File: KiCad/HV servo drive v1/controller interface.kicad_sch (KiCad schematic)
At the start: 46 parts, among them J8 8P8C_LED_Shielded_x2, M1 Fan_4pin, M2 Fan_4pin, SW2 TERM RES, U2 ISO6721BQDRQ1, U23 THVD1552, U3 ISO6721BQDRQ1, U4 ISO6721BQDRQ1, U6 AP64060QWU-7, U7 WRF0505S-3WR2

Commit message: KiCad 8.0 update
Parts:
- renumbered C95 to C1, C19 to C11, C92 to C13, C1 to C16, C93 to C18, C18 to C19, C11 to C2, C94 to C3, C2 to C31, C13 to C4, C91 to C5, C90 to C6, C16 to C7, C3 to C90, C4 to C91, C31 to C92, C5 to C93, C6 to C94, C7 to C95, J8 to J7, L17 to L1, L1 to L16, L5 to L17, L16 to L5, M2 to M1, M1 to M2, R5 to R1, R6 to R2, R90 to R3, R91 to R4, R4 to R5, R3 to R6, R2 to R79, R1 to R80, U6 to U2, U4 to U23, U23 to U3, U7 to U4, U2 to U6, U3 to U7

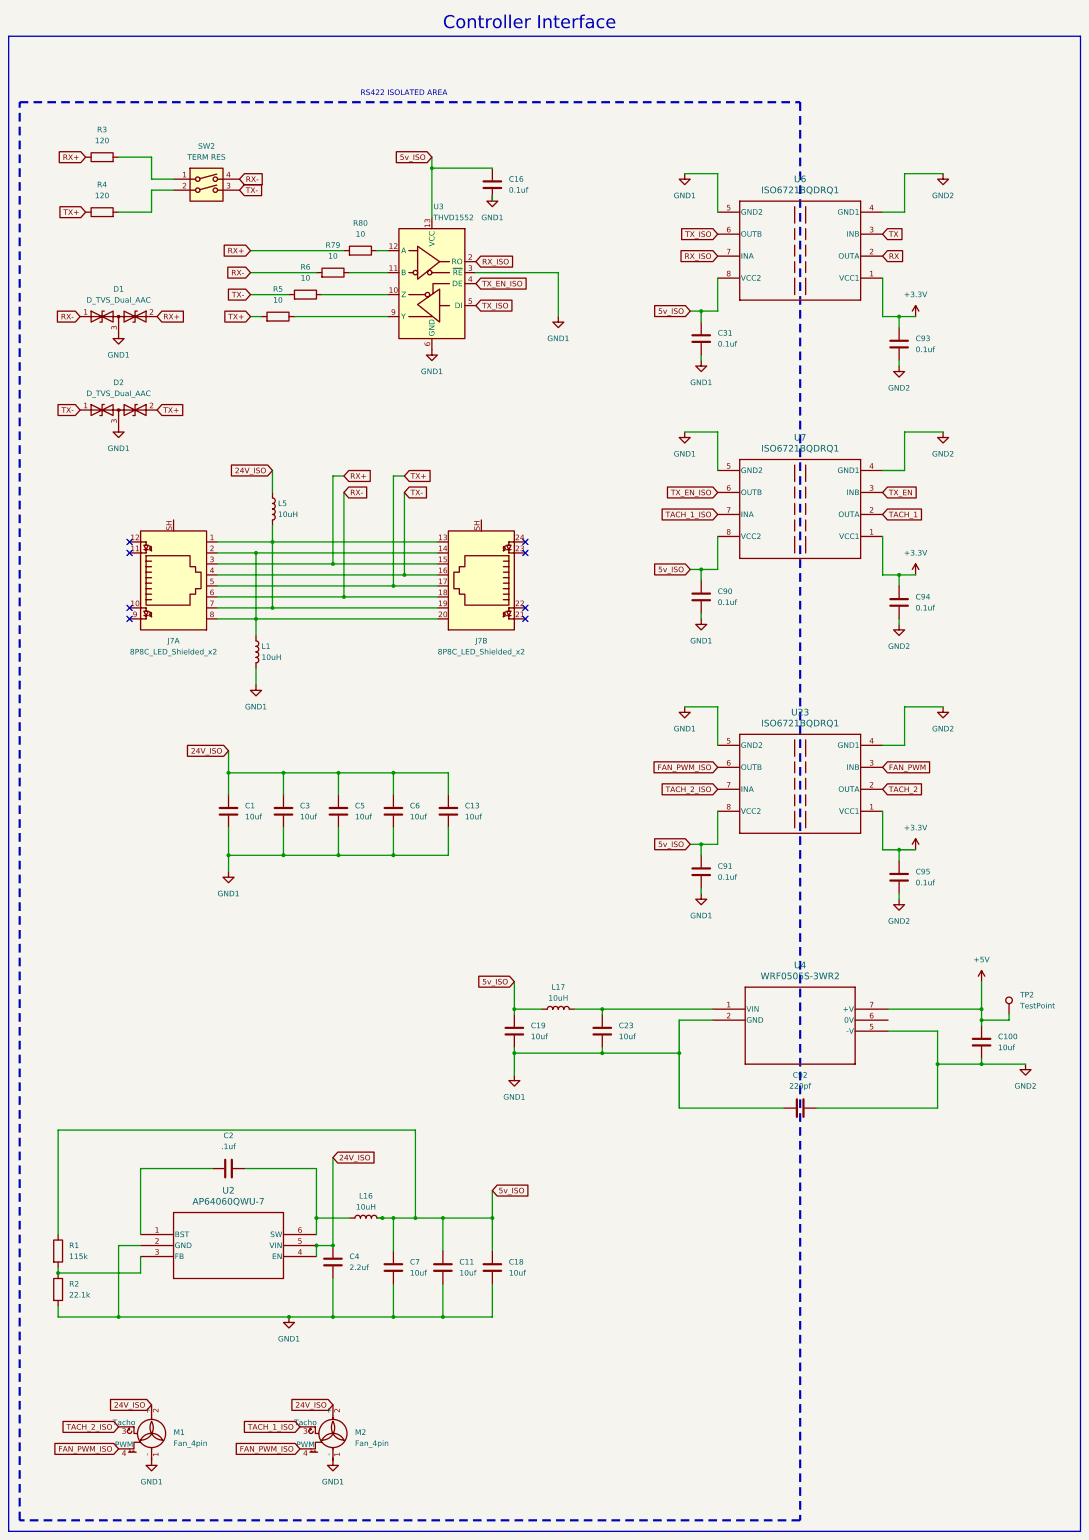
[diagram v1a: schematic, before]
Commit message: start rev 2 changes
fix component references, fix rj45 and dc-dc converter footprints, add RLC filters on all power connectors, add more mounting holes
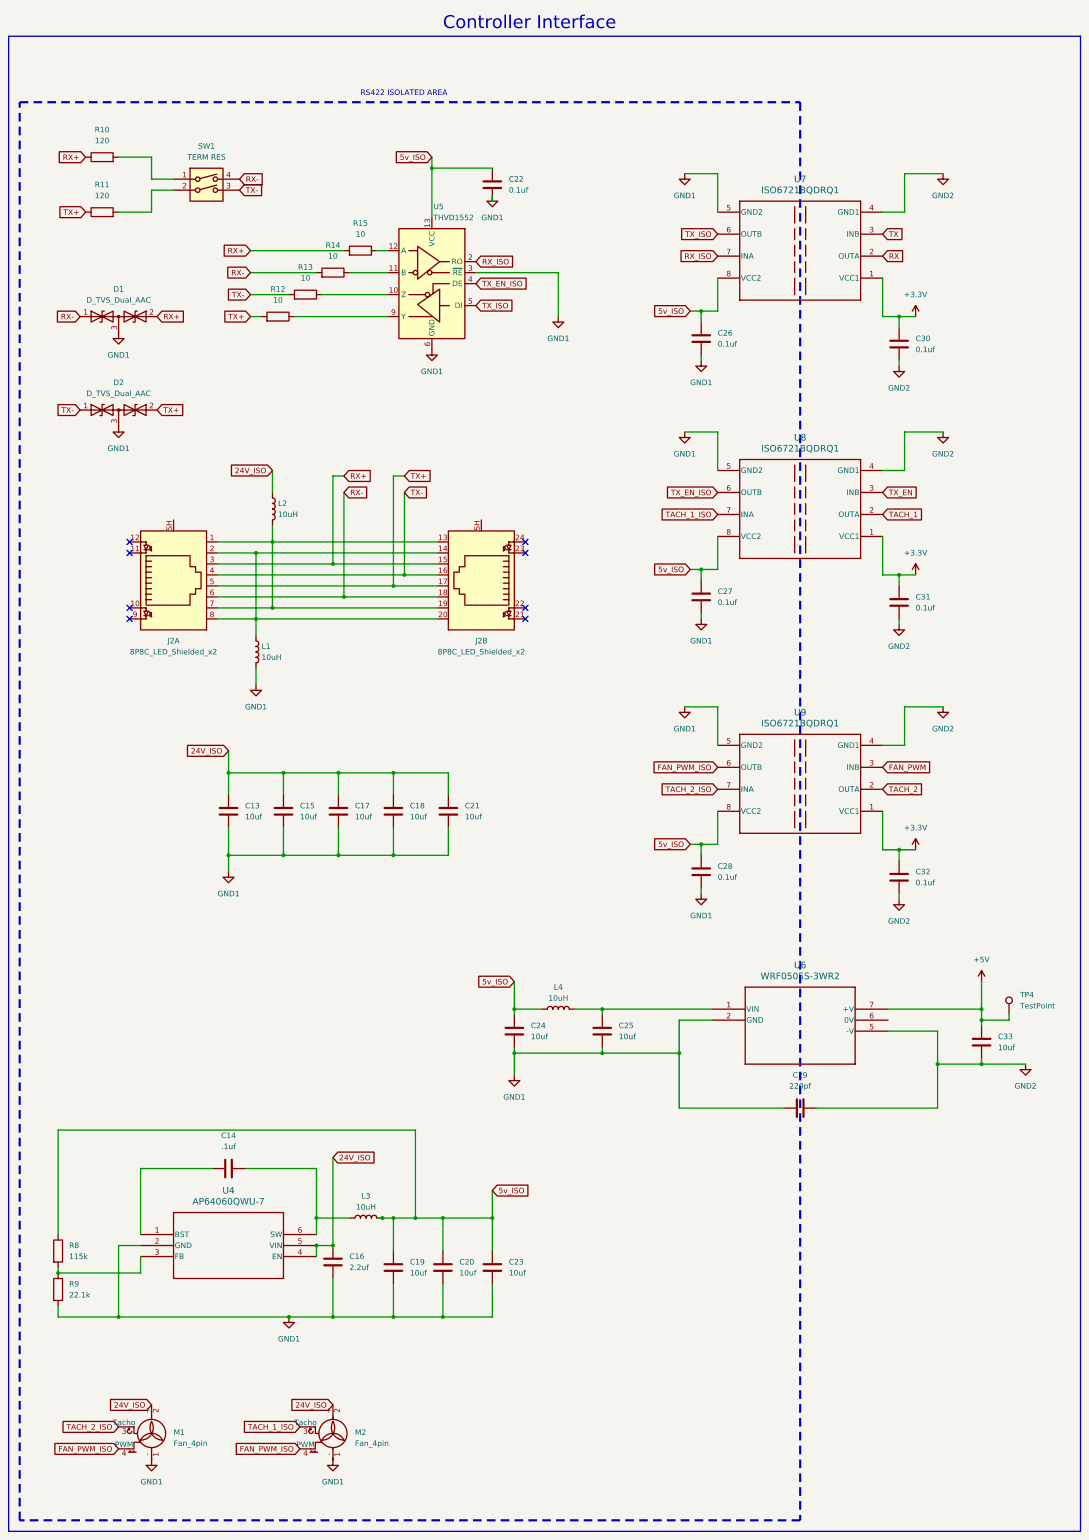
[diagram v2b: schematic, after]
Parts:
- renumbered C1 to C13, C2 to C14, C3 to C15, C4 to C16, C5 to C17, C6 to C18, C7 to C19, C11 to C20, C13 to C21, C16 to C22, C18 to C23, C19 to C24, C23 to C25, C31 to C26, C90 to C27, C91 to C28, C92 to C29, C93 to C30, C94 to C31, C95 to C32, C100 to C33, J7 to J2, L5 to L2, L16 to L3, L17 to L4, R3 to R10, R4 to R11, R5 to R12, R6 to R13, R79 to R14, R80 to R15, R1 to R8, R2 to R9, SW2 to SW1, TP2 to TP4, U2 to U4, U3 to U5, U4 to U6, U6 to U7, U7 to U8, U23 to U9

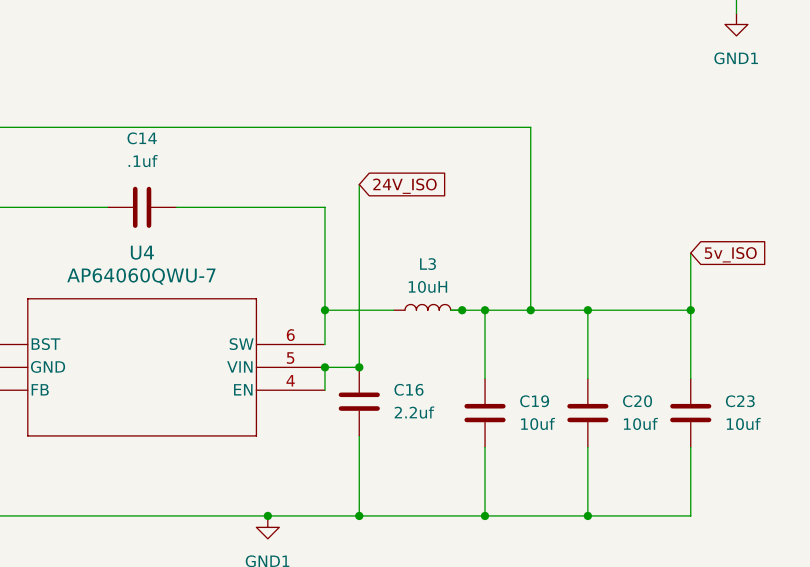
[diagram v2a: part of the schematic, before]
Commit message: round PCb edges
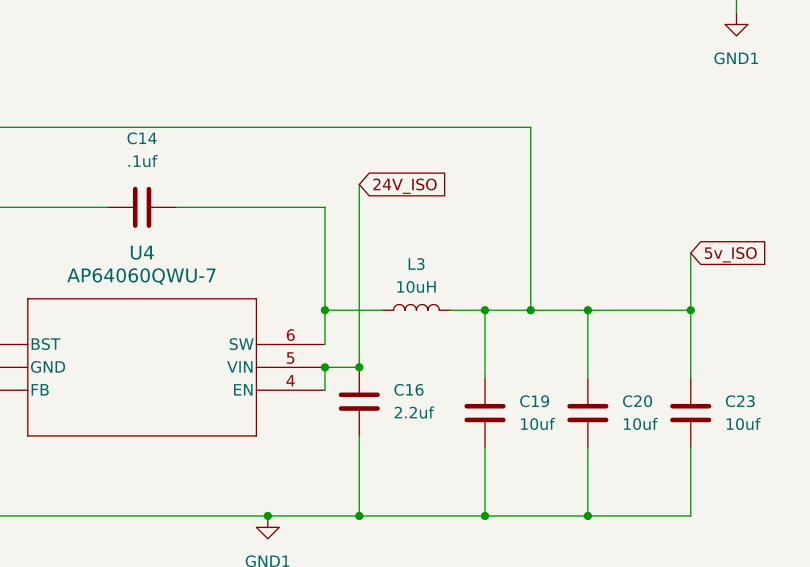
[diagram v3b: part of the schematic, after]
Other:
- moved on the sheet: L3
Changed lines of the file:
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@@
 	)
 	(junction
-		(at 266.7 308.61)
-		(diameter 0)
-		(color 0 0 0 0)
-	)
-	(junction
 		(at 255.27 331.47)
 		(diameter 0)
@@
 	(wire
 		(pts
-			(xy 265.43 308.61) (xy 266.7 308.61)
+			(xy 265.43 308.61) (xy 269.24 308.61)
 		)
 		(stroke
@@
 	(wire
 		(pts
-			(xy 251.46 308.61) (xy 259.08 308.61)
+			(xy 251.46 308.61) (xy 257.81 308.61)
 		)
 		(stroke
@@
 	(wire
 		(pts
-			(xy 266.7 308.61) (xy 269.24 308.61)
-		)
-		(stroke
-			(width 0)
-			(type default)
-		)
-	)
-	(wire
-		(pts
 			(xy 340.36 158.75) (xy 340.36 161.29)
 		)
@@
 	(symbol
 		(lib_id "Device:L")
-		(at 262.89 308.61 90)
+		(at 261.62 308.61 90)
 		(unit 1)
 		(exclude_from_sim no)
@@
 		(fields_autoplaced yes)
 		(property "Reference" "L3"
-			(at 262.89 303.53 90)
+			(at 261.62 303.53 90)
 			(effects
 				(font
@@
 		)
 		(property "Value" "10uH"
-			(at 262.89 306.07 90)
+			(at 261.62 306.07 90)
 			(effects
 				(font
@@
 		)
 		(property "Footprint" "Inductor_SMD:L_1008_2520Metric"
-			(at 262.89 308.61 0)
+			(at 261.62 308.61 0)
 			(effects
 				(font
@@
 		)
 		(property "Datasheet" "~"
-			(at 262.89 308.61 0)
+			(at 261.62 308.61 0)
 			(effects
 				(font
@@
 		)
 		(property "Description" ""
-			(at 262.89 308.61 0)
+			(at 261.62 308.61 0)
 			(effects
 				(font

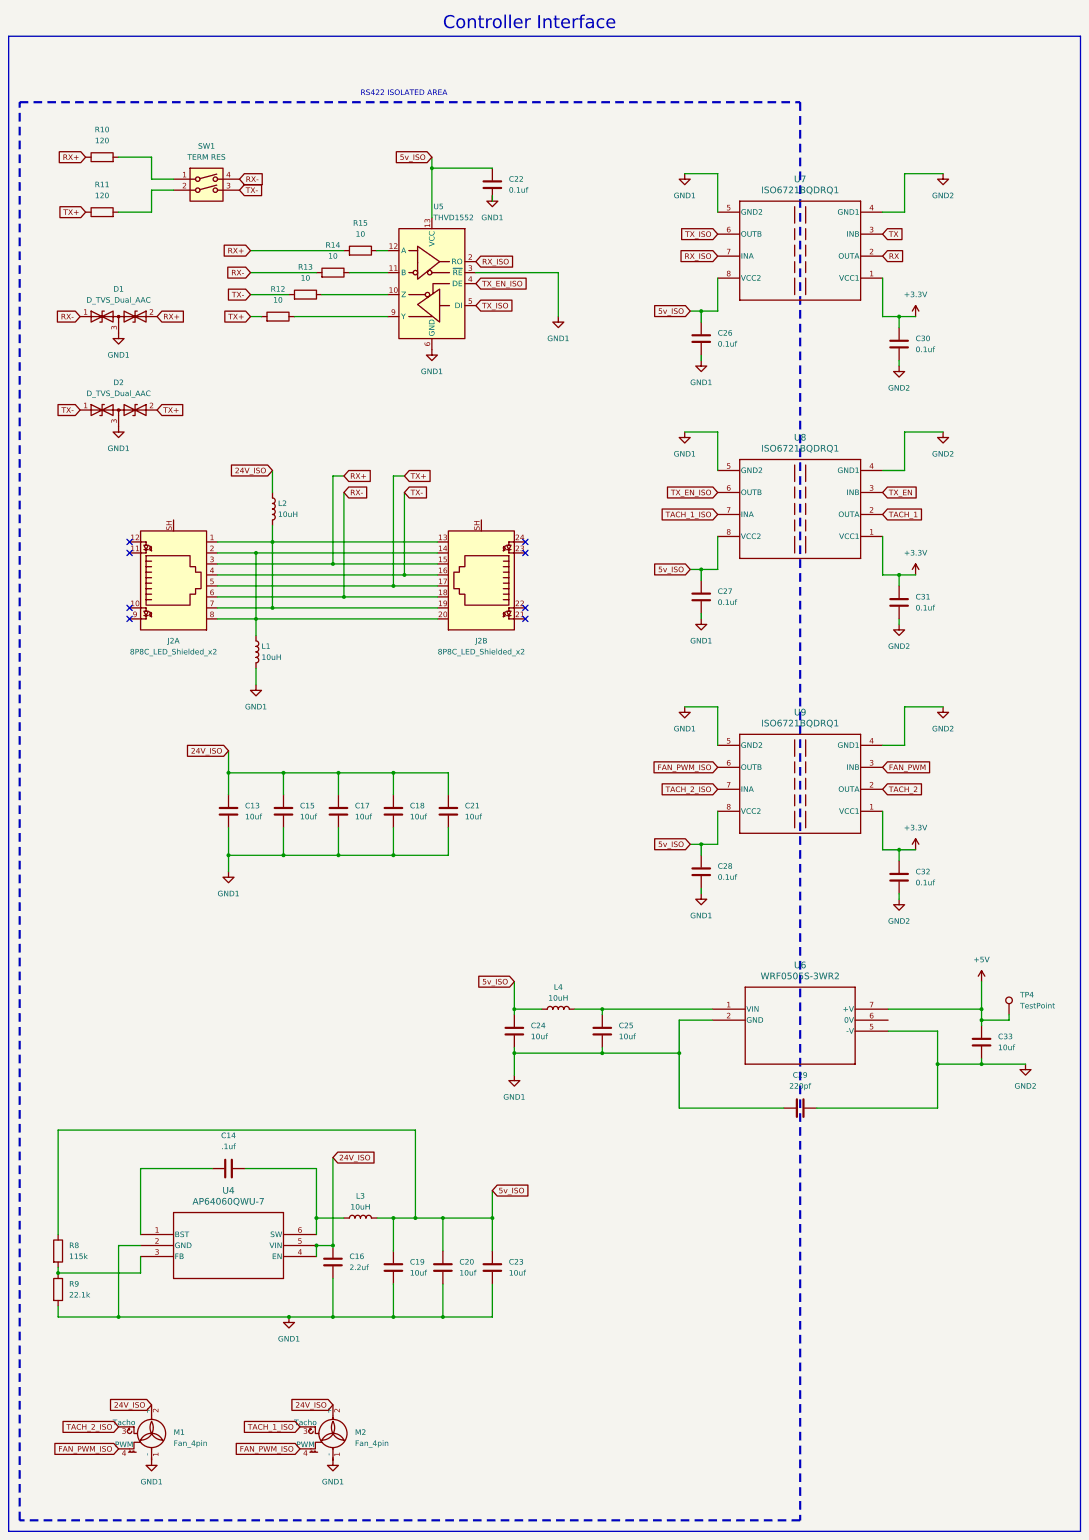
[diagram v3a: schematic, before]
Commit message: update to rev 2.1
basically the same version as in the FOC youtube video, with some minor issues fixed
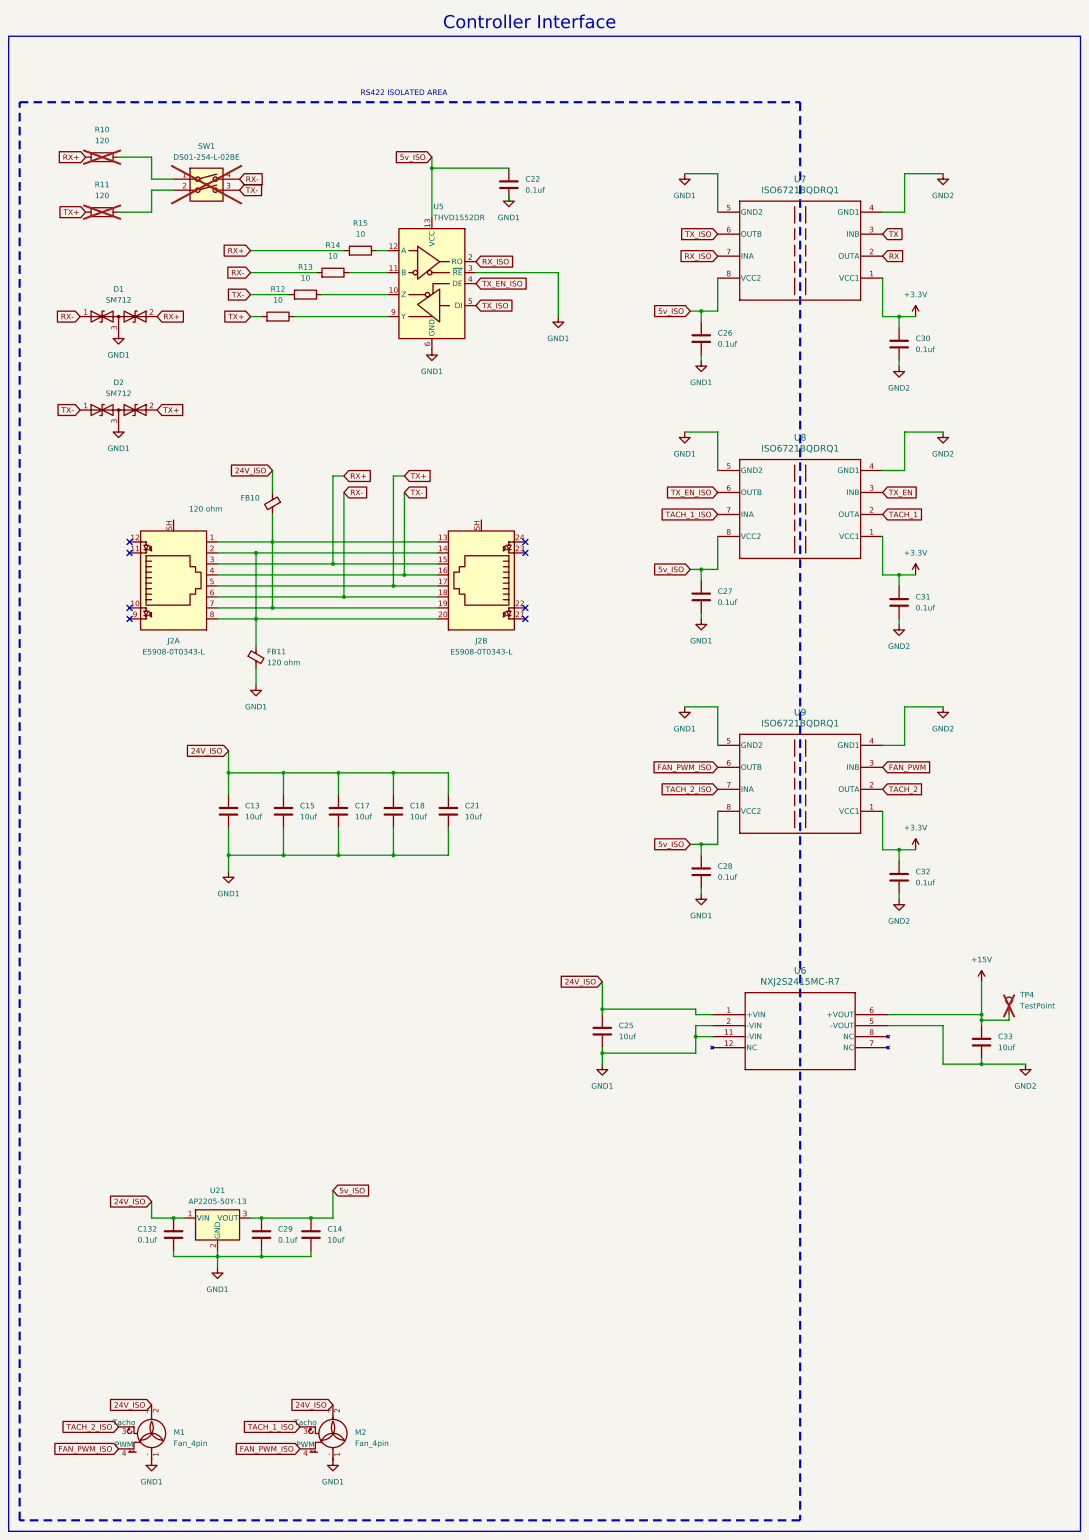
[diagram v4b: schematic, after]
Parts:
- removed C16: 2.2uf, Capacitor_SMD:C_0603_1608Metric, symbol Device:C
- removed C19, C20, C23, C24: 10uf, Capacitor_SMD:C_0805_2012Metric, symbol Device:C
- removed L1, L2, L3, L4: 10uH, Inductor_SMD:L_1008_2520Metric, symbol Device:L
- removed R8: 115k, Resistor_SMD:R_0603_1608Metric, symbol Device:R
- removed R9: 22.1k, Resistor_SMD:R_0603_1608Metric, symbol Device:R
- removed U4: AP64060QWU-7, footprints:IC6_AP64060QWU-7_DIO, symbol 2023-05-31_19-45-09:AP64060QWU-7
- removed U6: WRF0505S-3WR2, footprints:F0505S-2WR3, symbol F0505S DC-DC:F0505S
- added C132: 0.1uf, Capacitor_SMD:C_0603_1608Metric, symbol Device:C
- added FB10, FB11: 120 ohm, Inductor_SMD:L_0603_1608Metric, symbol Device:FerriteBead_Small
- added U21: AP2205-50Y-13, Package_TO_SOT_SMD:SOT-89-3, symbol Regulator_Linear:AP2204R-5.0
- added U6: NXJ2S2415MC-R7, footprints:NXJ2_24V_MUR, symbol NXJ2S2415MC-R7:NXJ2S2415MC-R7
- C13, C15, C17, C18, C21, C25, C33: Generic Allowed? (none) -> yes; Manufacturer (none) -> Murata Electronics; Part number (none) -> GRM21BR61H106KE43L
- C14: value .1uf -> 10uf; footprint Capacitor_SMD:C_0603_1608Metric -> Capacitor_SMD:C_0805_2012Metric; Generic Allowed? (none) -> yes; Manufacturer (none) -> Murata Electronics; Part number (none) -> GRM21BR61H106KE43L
- C22, C26, C27, C28, C30, C31, C32: Generic Allowed? (none) -> yes; Manufacturer (none) -> YAGEO; Part number (none) -> CC0603ZRY5V9BB104
- C29: value 220pf -> 0.1uf; footprint Capacitor_THT:C_Disc_D7.5mm_W5.0mm_P10.00mm -> Capacitor_SMD:C_0603_1608Metric; Generic Allowed? (none) -> yes; Manufacturer (none) -> YAGEO; Part number (none) -> CC0603ZRY5V9BB104
- D1, D2: value D_TVS_Dual_AAC -> SM712; Generic Allowed? (none) -> yes; Manufacturer (none) -> SMC Diode Solutions; Part number (none) -> SM712
- J2: value 8P8C_LED_Shielded_x2 -> E5908-0T0343-L; Generic Allowed? (none) -> yes; Manufacturer (none) -> Pulse Electronics; Part number (none) -> E5908-0T0343-L
- M1, M2: Generic Allowed? (none) -> yes; Manufacturer (none) -> Molex; Part number (none) -> 0022035045
- R10, R11: Generic Allowed? (none) -> yes; Manufacturer (none) -> YAGEO; Part number (none) -> RC0603JR-07120RL; now not fitted
- R12, R13, R14, R15: Generic Allowed? (none) -> yes; Manufacturer (none) -> Stackpole Electronics Inc; Part number (none) -> RMCF0603FT10R0
- SW1: value TERM RES -> DS01-254-L-02BE; Generic Allowed? (none) -> yes; Manufacturer (none) -> Same Sky (Formerly CUI Devices); Part number (none) -> DS01-254-L-02BE; now not fitted
- TP4: now not fitted
- U5: value THVD1552 -> THVD1552DR; Generic Allowed? (none) -> no; Manufacturer (none) -> Texas Instruments; Part number (none) -> THVD1552DR
- U7, U8, U9: Generic Allowed? (none) -> yes; Manufacturer (none) -> Texas Instruments; Part number (none) -> ISO6721BQDRQ1
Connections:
- net 24V_ISO: now also C25.1, C132.1, FB10.1, U21.1 (VIN), U6.1 (+VIN)
- net 5v_ISO: now also C14.1, C29.2, U21.3 (VOUT)
- net GND1: now also C14.2, C29.1, C132.2, FB11.2, U21.2 (GND), U6.11 (-VIN), U6.2 (-VIN); no longer C29.2
- net GND2: now also U6.5 (-VOUT); no longer C29.1
- net at J2.1, J2.13, J2.19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: now also FB10.2
- net at J2.14, J2.2, J2.20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: now also FB11.1
- net +5V renamed +15V
- net +15V: now also U6.6 (+VOUT)
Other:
- moved on the sheet: C22
